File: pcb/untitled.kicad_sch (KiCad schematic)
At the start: 15 parts, among them IC3 AD844ANZ, IC5 FOD814SD, U2 REF192GSZ

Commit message: first bulk commit of routing
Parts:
- removed C22: 10u, capstone:CAPPM7343X310N-10u, symbol capstone:T495X106K050ATE250-10u
- removed C23, C24: 0.22u, capstone:C0805-0.22u, symbol capstone:C0805C224M5VACTU-0.22u
- removed IC3: AD844ANZ, capstone:DIP794W56P254L959H533Q8N-AD844-DIP8TH, symbol capstone:AD844ANZ
- added C22, C23, C24: 10u, capstone:T495D, symbol capstone:T495D106K035ATE300
- added C28, C32, C34, C38: 0.1u, capstone:CAPC220145_88N_KEM-0.1u, symbol capstone:C0805C104K5RAC7210
- added C29, C30, C35, C36, C39, C40: 0.22u, capstone:C0805-0.22u, symbol capstone:C0805C224M5VACTU-0.22u
- added C31, C37: 1u, capstone:C0805-1u, symbol capstone:C0805C105Z5VACTU-1u
- added IC10: AD844_OPAMP_MEL, capstone:SOIC127P1032X265-16N-AD844, symbol capstone:AD844JRZ-16-REEL7
- added IC3: FOD814_OPTO_NOSHD, capstone:SOP254P1016X385-4N-FOD, symbol capstone:FOD814SD
- added IC6: AD844_OPAMP_AL, capstone:SOIC127P1032X265-16N-AD844, symbol capstone:AD844JRZ-16-REEL7
- added IC7: FOD814_OPTO_AL, capstone:SOP254P1016X385-4N-FOD, symbol capstone:FOD814SD
- added IC8: AD844_OPAMP_NOSHD, capstone:SOIC127P1032X265-16N-AD844, symbol capstone:AD844JRZ-16-REEL7
- added J_AD844: Conn_01x04, Connector_PinHeader_2.54mm:PinHeader_1x04_P2.54mm_Horizontal, symbol Connector_Generic:Conn_01x04
- added J_FOD814: Conn_01x06, Connector_PinHeader_2.54mm:PinHeader_1x06_P2.54mm_Horizontal, symbol Connector_Generic:Conn_01x06
- added J_REF192: Conn_01x03, Connector_PinHeader_2.54mm:PinHeader_1x03_P2.54mm_Horizontal, symbol Connector_Generic:Conn_01x03
- added R22, R28, R34: 1k, Resistor_SMD:R_0402_1005Metric, symbol Device:R
- added R23: 200, Resistor_SMD:R_0402_1005Metric, symbol Device:R
- added R24: 47, Resistor_SMD:R_0402_1005Metric, symbol Device:R
- added R25, R31, R35: 100k, Resistor_SMD:R_0402_1005Metric, symbol Device:R
- added R26, R27, R29, R30: 100, Resistor_SMD:R_0402_1005Metric, symbol Device:R
- added U3: REF192_AL, capstone:R_8_ADI-REF, symbol capstone:REF192GSZ
- added U4: REF192_MEL, capstone:R_8_ADI-REF, symbol capstone:REF192GSZ
- IC5: value FOD814SD -> FOD814_OPTO_MEL
- R15: value 10k -> 200
- R16, R20: value 100 -> 47
- R17: value 200 -> 100
- R19: value 47 -> 200
- U2: value REF192GSZ -> REF192_NOSHD
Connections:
- net Signal Gen is gone; now on net +5V: R17.2
- net +5V: now also C22.1 (+), C23.1 (+), C24.1 (+), C28.1, C30.1, C34.1, C36.1, C40.1, IC10.14 (V+), IC6.14 (V+), IC8.14 (V+), R26.2, R29.2, U3.2 (VS), U3.3 (*SLEEP), U4.2 (VS), U4.3 (*SLEEP); no longer R18.2
- net GND: now also R16.2, R18.1, R20.2, C22.2 (-), C23.2 (-), C24.2 (-), C28.2, C29.2, C30.2, C31.2, C32.2, C34.2, C35.2, C36.2, C37.2, C38.2, C39.2, C40.2, R22.1, R24.2, R27.1, R28.1, R30.1, R34.1, U3.4 (GND), U4.4 (GND); no longer R16.1, R19.1, R20.1
- net ADC1_IN13_OPTO_E_MEL: now reaches IC5.3 (E)
- net ADC1_IN13_OPTO_E_MEL: now also J_FOD814.5 (Pin_5), R30.2; no longer R20.2
- net at IC5.4 (C): now also R29.1; no longer R18.1
- net at R15.1: now also IC3.1 (AK)
- net Signal Output: now reaches R15.2
- net Signal Output: now also R19.2, IC10.5 (+IN), IC6.5 (+IN), IC8.5 (+IN), J_AD844.4 (Pin_4), R23.2; no longer R16.2
- net at IC5.1 (AK): now also R19.1; no longer R17.1
- net ADC1_IN12_OPTO_F_MEL: now reaches IC5.2 (KA)
- net ADC1_IN12_OPTO_F_MEL: now also R20.1, J_FOD814.6 (Pin_6); no longer R19.2
- net 2.5V renamed ADC1_IN4_VREF_NOSHD
- net ADC1_IN4_VREF_NOSHD: now also J_REF192.1 (Pin_1)
- new net: IC10.3 (-IN), R28.2, R31.2
- new net: IC6.3 (-IN), R22.2, R25.2
- new net: IC7.4 (C), R26.1
- new net: IC8.3 (-IN), R34.2, R35.2
- new net: IC7.1 (AK), R23.1
- new net: IC3.4 (C), R17.1
- new net -5V Output: C29.1, C35.1, C39.1, IC10.7 (V-), IC6.7 (V-), IC8.7 (V-)
- new net ADC1_IN10_OPTO_F_NOSHD: IC3.2 (KA), J_FOD814.2 (Pin_2), R16.1
- new net ADC1_IN11_OPTO_E_NOSHD: IC3.3 (E), J_FOD814.1 (Pin_1), R18.2
- new net ADC1_IN14_OPTO_F_AL: IC7.2 (KA), J_FOD814.4 (Pin_4), R24.1
- new net ADC1_IN15_OPTO_E_AL: IC7.3 (E), J_FOD814.3 (Pin_3), R27.2
- new net ADC1_IN1_OPAMP_NOSHD: IC8.12 (OUTPUT), J_AD844.1 (Pin_1), R35.1
- new net ADC1_IN2_OPAMP_MEL: IC10.12 (OUTPUT), J_AD844.3 (Pin_3), R31.1
- new net ADC1_IN3_OPAMP_AL: IC6.12 (OUTPUT), J_AD844.2 (Pin_2), R25.1
- new net ADC1_IN5_VREF_MEL: C37.1, C38.1, J_REF192.3 (Pin_3), U4.6 (OUTPUT)
- new net ADC1_IN6_VREF_AL: C31.1, C32.1, J_REF192.2 (Pin_2), U3.6 (OUTPUT)
- no-connect marks 5 -> 39
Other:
- moved on the sheet: C19, C20, C21, U2

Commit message: Wire touchup, initial changes (#12)
* Implemented mosfet, decoupling

Please review functionality

* wire placement, inital revisions

made it more PCB ready with spacing and such
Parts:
- R22, R28, R34: value 1k -> 100k
- R25, R31, R35: value 100k -> 1k
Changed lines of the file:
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@@
   (junction (at 97.79 125.73) (diameter 0) (color 0 0 0 0)
   )
+  (junction (at 160.02 34.29) (diameter 0) (color 0 0 0 0)
+  )
+  (junction (at 165.1 165.1) (diameter 0) (color 0 0 0 0)
+  )
+  (junction (at 232.41 104.14) (diameter 0) (color 0 0 0 0)
+  )
+  (junction (at 323.85 113.03) (diameter 0) (color 0 0 0 0)
+  )
+  (junction (at 167.64 101.6) (diameter 0) (color 0 0 0 0)
+  )
+  (junction (at 234.95 104.14) (diameter 0) (color 0 0 0 0)
+  )
+  (junction (at 322.58 55.88) (diameter 0) (color 0 0 0 0)
+  )
+  (junction (at 299.72 55.88) (diameter 0) (color 0 0 0 0)
+  )
+  (junction (at 224.79 104.14) (diameter 0) (color 0 0 0 0)
+  )
+  (junction (at 171.45 101.6) (diameter 0) (color 0 0 0 0)
+  )
+  (junction (at 107.95 125.73) (diameter 0) (color 0 0 0 0)
+  )
+  (junction (at 240.03 36.83) (diameter 0) (color 0 0 0 0)
+  )
+  (junction (at 97.79 186.69) (diameter 0) (color 0 0 0 0)
+  )
+  (junction (at 233.68 167.64) (diameter 0) (color 0 0 0 0)
+  )
+  (junction (at 322.58 163.83) (diameter 0) (color 0 0 0 0)
+  )
+  (junction (at 43.18 62.23) (diameter 0) (color 0 0 0 0)
+  )
+  (junction (at 109.22 57.15) (diameter 0) (color 0 0 0 0)
+  )
   (junction (at 45.72 52.07) (diameter 0) (color 0 0 0 0)
-  )
-  (junction (at 160.02 34.29) (diameter 0) (color 0 0 0 0)
-  )
-  (junction (at 165.1 165.1) (diameter 0) (color 0 0 0 0)
-  )
-  (junction (at 232.41 104.14) (diameter 0) (color 0 0 0 0)
-  )
-  (junction (at 323.85 113.03) (diameter 0) (color 0 0 0 0)
-  )
-  (junction (at 167.64 101.6) (diameter 0) (color 0 0 0 0)
-  )
-  (junction (at 234.95 104.14) (diameter 0) (color 0 0 0 0)
-  )
-  (junction (at 322.58 55.88) (diameter 0) (color 0 0 0 0)
-  )
-  (junction (at 299.72 55.88) (diameter 0) (color 0 0 0 0)
-  )
-  (junction (at 224.79 104.14) (diameter 0) (color 0 0 0 0)
-  )
-  (junction (at 171.45 101.6) (diameter 0) (color 0 0 0 0)
-  )
-  (junction (at 107.95 125.73) (diameter 0) (color 0 0 0 0)
-  )
-  (junction (at 240.03 36.83) (diameter 0) (color 0 0 0 0)
-  )
-  (junction (at 97.79 186.69) (diameter 0) (color 0 0 0 0)
-  )
-  (junction (at 233.68 167.64) (diameter 0) (color 0 0 0 0)
-  )
-  (junction (at 322.58 163.83) (diameter 0) (color 0 0 0 0)
-  )
-  (junction (at 43.18 62.23) (diameter 0) (color 0 0 0 0)
-  )
-  (junction (at 109.22 57.15) (diameter 0) (color 0 0 0 0)
   )
   (no_connect (at 46.99 118.11))
@@
     (stroke (width 0) (type default))
   )
+  (wire (pts (xy 76.2 25.4) (xy 109.22 25.4))
+    (stroke (width 0) (type default))
+  )
   (wire (pts (xy 233.68 140.97) (xy 233.68 167.64))
     (stroke (width 0) (type default))
@@
     (stroke (width 0) (type default))
   )
-  (wire (pts (xy 76.2 25.4) (xy 109.22 25.4))
-    (stroke (width 0) (type default))
-  )
   (wire (pts (xy 97.79 186.69) (xy 95.25 186.69))
     (stroke (width 0) (type default))
@@
     (stroke (width 0) (type default))
   )
+  (wire (pts (xy 45.72 25.4) (xy 68.58 25.4))
+    (stroke (width 0) (type default))
+  )
   (wire (pts (xy 97.79 114.3) (xy 97.79 120.65))
     (stroke (width 0) (type default))
@@
     (stroke (width 0) (type default))
   )
+  (wire (pts (xy 43.18 52.07) (xy 45.72 52.07))
+    (stroke (width 0) (type default))
+  )
   (wire (pts (xy 299.72 153.67) (xy 295.91 153.67))
     (stroke (width 0) (type default))
@@
     (stroke (width 0) (type default))
   )
+  (wire (pts (xy 33.02 52.07) (xy 35.56 52.07))
+    (stroke (width 0) (type default))
+  )
   (wire (pts (xy 109.22 25.4) (xy 109.22 57.15))
     (stroke (width 0) (type default))
@@
     (stroke (width 0) (type default))
   )
-  (wire (pts (xy 33.02 52.07) (xy 35.56 52.07))
-    (stroke (width 0) (type default))
-  )
   (wire (pts (xy 232.41 104.14) (xy 232.41 110.49))
     (stroke (width 0) (type default))
@@
     (stroke (width 0) (type default))
   )
-  (wire (pts (xy 43.18 52.07) (xy 45.72 52.07))
-    (stroke (width 0) (type default))
-  )
   (wire (pts (xy 107.95 191.77) (xy 119.38 191.77))
     (stroke (width 0) (type default))
@@
   )
   (wire (pts (xy 222.25 184.15) (xy 222.25 190.5))
-    (stroke (width 0) (type default))
-  )
-  (wire (pts (xy 68.58 25.4) (xy 45.72 25.4))
     (stroke (width 0) (type default))
   )
@@
       (effects (font (size 1.27 1.27)))
     )
-    (property "Value" "1k" (at 38.1 184.15 90)
+    (property "Value" "100k" (at 38.1 184.15 90)
       (effects (font (size 1.27 1.27)))
     )
@@
       (effects (font (size 1.27 1.27)))
     )
-    (property "Value" "1k" (at 38.1 118.11 90)
+    (property "Value" "100k" (at 38.1 118.11 90)
       (effects (font (size 1.27 1.27)))
     )
@@
       (effects (font (size 1.27 1.27)) (justify left))
     )
-    (property "Value" "100k" (at 69.85 99.06 90)
+    (property "Value" "1k" (at 69.85 99.06 90)
       (effects (font (size 1.27 1.27)) (justify left))
     )
@@
       (effects (font (size 1.27 1.27)))
     )
-    (property "Value" "1k" (at 39.37 49.53 90)
+    (property "Value" "100k" (at 39.37 49.53 90)
       (effects (font (size 1.27 1.27)))
     )
@@
       (effects (font (size 1.27 1.27)) (justify left))
     )
-    (property "Value" "100k" (at 71.12 30.48 90)
+    (property "Value" "1k" (at 71.12 30.48 90)
       (effects (font (size 1.27 1.27)) (justify left))
     )
@@
       (effects (font (size 1.27 1.27)) (justify left))
     )
-    (property "Value" "100k" (at 69.85 165.1 90)
-      (effects (font (size 1.27 1.27)) (justify left))
-    )
+    (property "Value" "1k" (at 69.85 165.1 90)
+      (effects (font (size 1.27 1.27)) (justify left))
+    )

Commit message: done layout/ratsnet
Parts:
- J_AD844: footprint Connector_PinHeader_2.54mm:PinHeader_1x04_P2.54mm_Horizontal -> Connector_PinHeader_2.54mm:PinHeader_1x04_P2.54mm_Vertical
- J_FOD814: footprint Connector_PinHeader_2.54mm:PinHeader_1x06_P2.54mm_Horizontal -> Connector_PinHeader_2.54mm:PinHeader_1x06_P2.54mm_Vertical
- J_REF192: footprint Connector_PinHeader_2.54mm:PinHeader_1x03_P2.54mm_Horizontal -> Connector_PinHeader_2.54mm:PinHeader_1x03_P2.54mm_Vertical
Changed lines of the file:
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@@
       (effects (font (size 1.27 1.27)) (justify left))
     )
-    (property "Footprint" "Connector_PinHeader_2.54mm:PinHeader_1x06_P2.54mm_Horizontal" (at 377.19 123.19 0)
+    (property "Footprint" "Connector_PinHeader_2.54mm:PinHeader_1x06_P2.54mm_Vertical" (at 377.19 123.19 0)
       (effects (font (size 1.27 1.27)) hide)
     )
@@
       (effects (font (size 1.27 1.27)) (justify left))
     )
-    (property "Footprint" "Connector_PinHeader_2.54mm:PinHeader_1x03_P2.54mm_Horizontal" (at 265.43 81.28 0)
+    (property "Footprint" "Connector_PinHeader_2.54mm:PinHeader_1x03_P2.54mm_Vertical" (at 265.43 81.28 0)
       (effects (font (size 1.27 1.27)) hide)
     )
@@
       (effects (font (size 1.27 1.27)) (justify left))
     )
-    (property "Footprint" "Connector_PinHeader_2.54mm:PinHeader_1x04_P2.54mm_Horizontal" (at 133.35 102.87 0)
-      (effects (font (size 1.27 1.27)) hide)
-    )
+    (property "Footprint" "Connector_PinHeader_2.54mm:PinHeader_1x04_P2.54mm_Vertical" (at 133.35 102.87 0)
+      (effects (font (size 1.27 1.27)) hide)
+    )

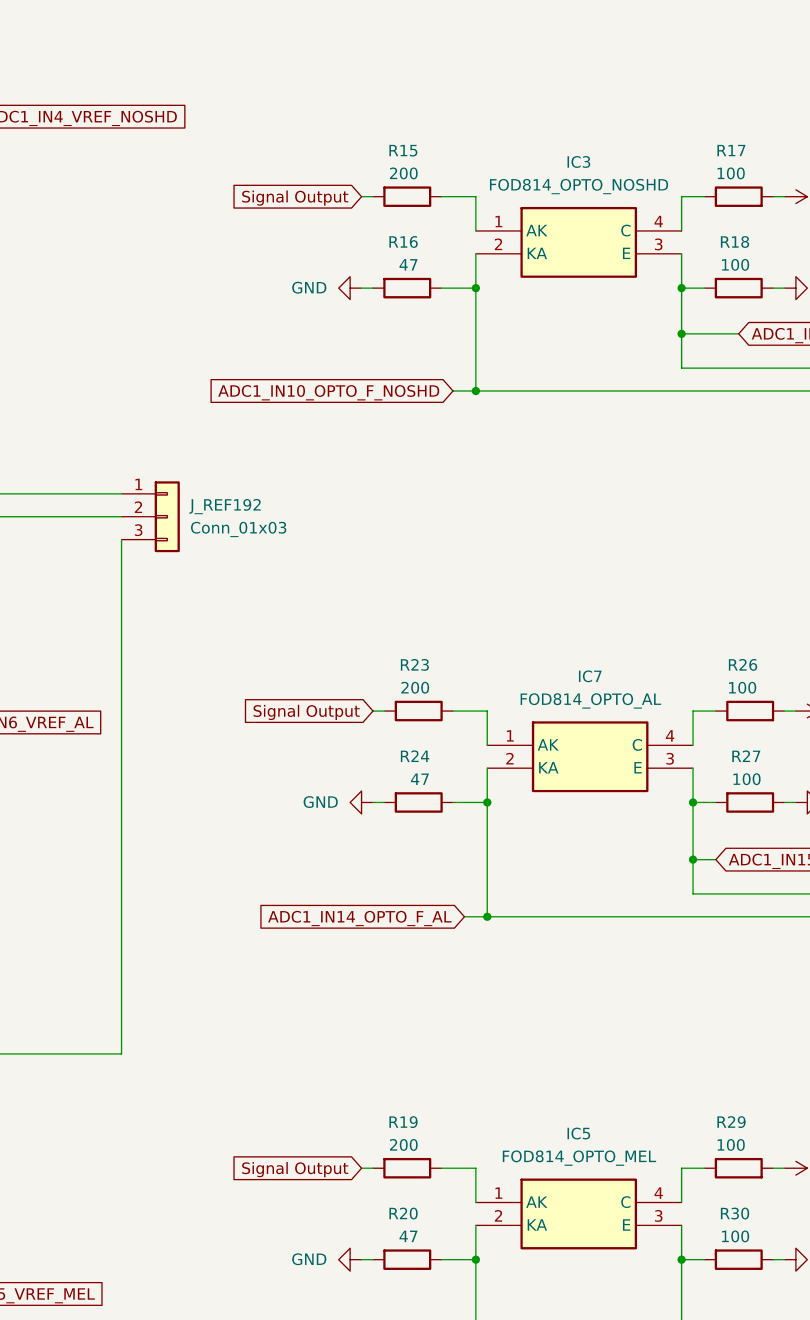
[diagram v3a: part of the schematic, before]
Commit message: Added-Voltage-follower-and-Changed-opto-resistor-values
Added the voltage follower circuit to the signal gen. Changed the R values on the optoisolator circuit.
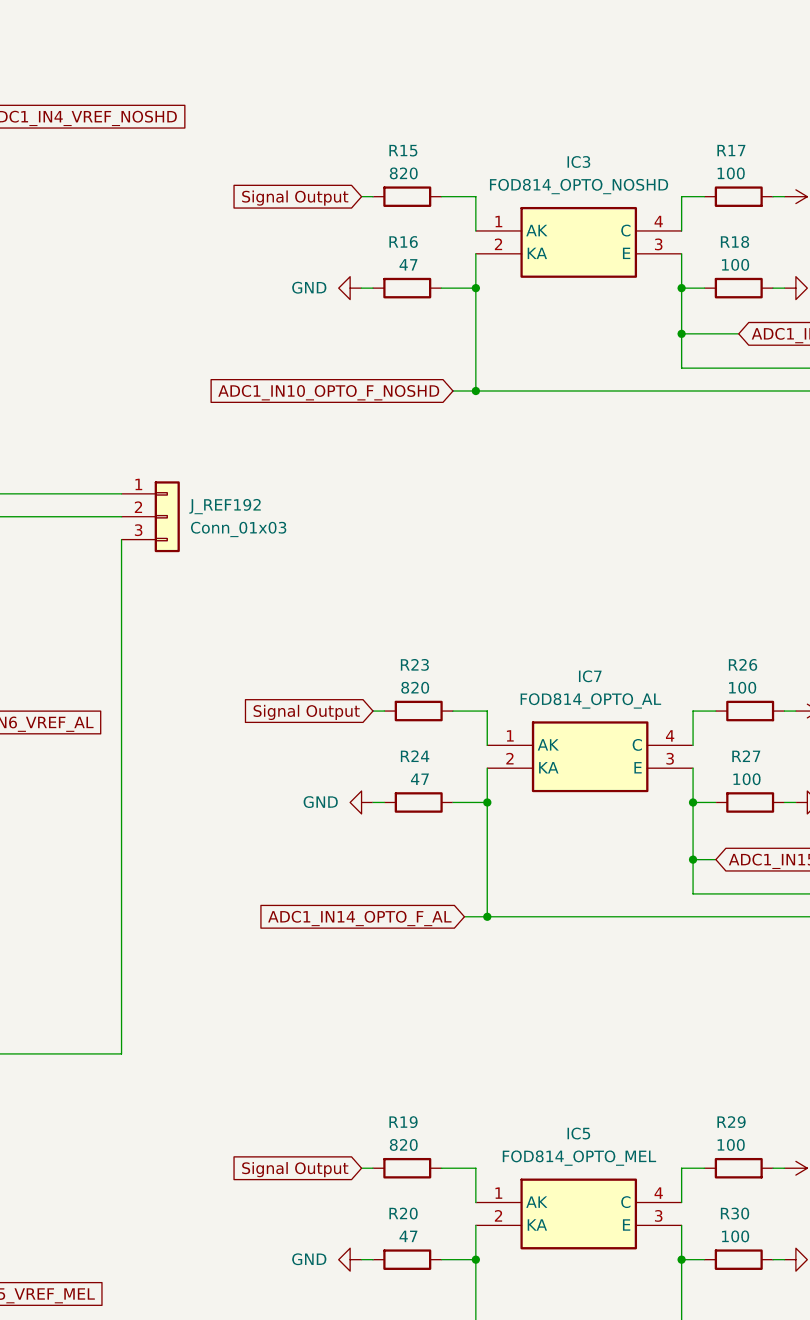
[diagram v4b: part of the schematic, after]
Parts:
- R15, R19, R23: value 200 -> 820
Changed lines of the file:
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@@
       (effects (font (size 1.27 1.27)) (justify right))
     )
-    (property "Value" "200" (at 293.37 43.18 90)
+    (property "Value" "820" (at 293.37 43.18 90)
       (effects (font (size 1.27 1.27)) (justify right))
     )
@@
       (effects (font (size 1.27 1.27)) (justify right))
     )
-    (property "Value" "200" (at 293.37 151.13 90)
+    (property "Value" "820" (at 293.37 151.13 90)
       (effects (font (size 1.27 1.27)) (justify right))
     )
@@
       (effects (font (size 1.27 1.27)) (justify right))
     )
-    (property "Value" "200" (at 294.64 100.33 90)
-      (effects (font (size 1.27 1.27)) (justify right))
-    )
+    (property "Value" "820" (at 294.64 100.33 90)
+      (effects (font (size 1.27 1.27)) (justify right))
+    )
